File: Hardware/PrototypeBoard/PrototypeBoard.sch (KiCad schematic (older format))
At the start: 10 parts

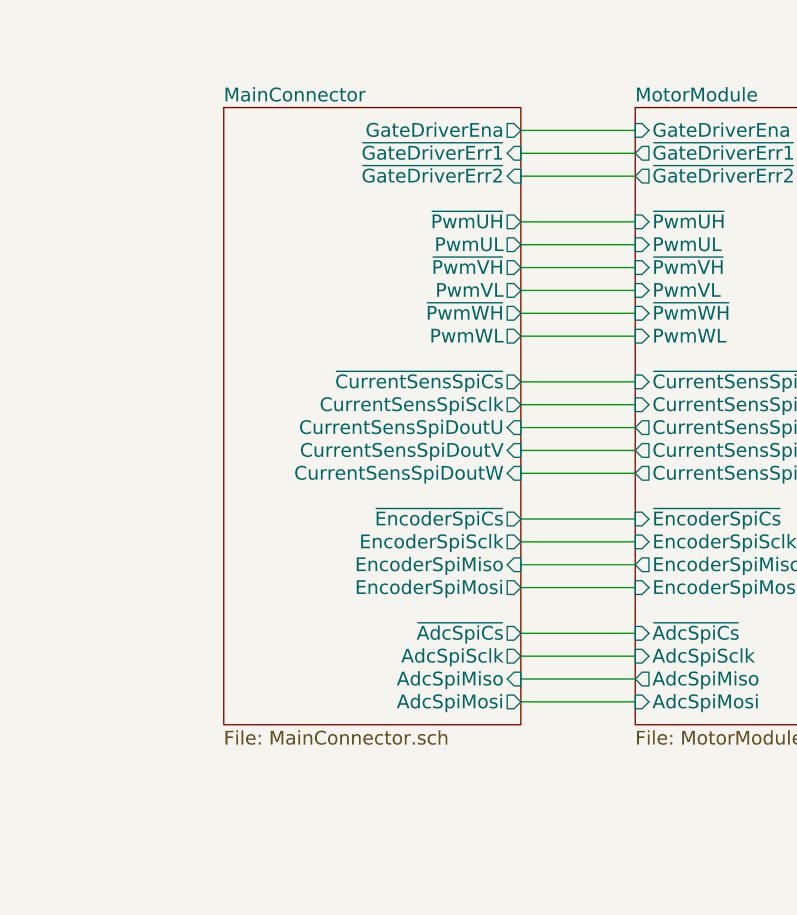
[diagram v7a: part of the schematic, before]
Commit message: Added LEDs for PWM, SPI communication, Gate Driver Errors and Gate Driver disabled
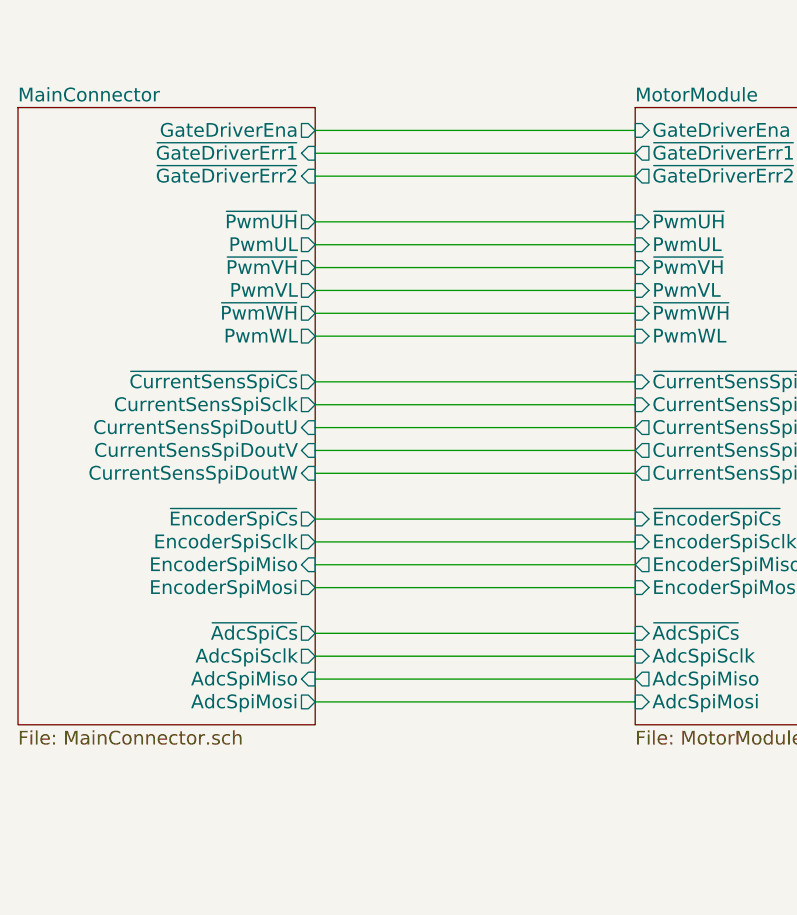
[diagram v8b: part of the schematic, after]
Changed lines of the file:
@@
 $EndSheet
 $Sheet
-S 4500 1800 1300 2700
+S 3600 1800 1300 2700
 U 5AFD76B5
 F0 "MainConnector" 60
 F1 "MainConnector.sch" 60
-F2 "GateDriverEna" O R 5800 1900 60
-F3 "~GateDriverErr1" I R 5800 2000 60
-F4 "~GateDriverErr2" I R 5800 2100 60
-F5 "~PwmUH" O R 5800 2300 60
-F6 "PwmUL" O R 5800 2400 60
-F7 "~PwmVH" O R 5800 2500 60
-F8 "PwmVL" O R 5800 2600 60
-F9 "~PwmWH" O R 5800 2700 60
-F10 "PwmWL" O R 5800 2800 60
-F11 "~CurrentSensSpiCs" O R 5800 3000 60
-F12 "CurrentSensSpiSclk" O R 5800 3100 60
-F13 "CurrentSensSpiDoutU" I R 5800 3200 60
-F14 "CurrentSensSpiDoutV" I R 5800 3300 60
-F15 "CurrentSensSpiDoutW" I R 5800 3400 60
-F16 "~EncoderSpiCs" O R 5800 3600 60
-F17 "EncoderSpiSclk" O R 5800 3700 60
-F18 "EncoderSpiMiso" I R 5800 3800 60
-F19 "EncoderSpiMosi" O R 5800 3900 60
-F20 "~AdcSpiCs" O R 5800 4100 60
-F21 "AdcSpiSclk" O R 5800 4200 60
-F22 "AdcSpiMiso" I R 5800 4300 60
-F23 "AdcSpiMosi" O R 5800 4400 60
+F2 "GateDriverEna" O R 4900 1900 60
+F3 "~GateDriverErr1" I R 4900 2000 60
+F4 "~GateDriverErr2" I R 4900 2100 60
+F5 "~PwmUH" O R 4900 2300 60
+F6 "PwmUL" O R 4900 2400 60
+F7 "~PwmVH" O R 4900 2500 60
+F8 "PwmVL" O R 4900 2600 60
+F9 "~PwmWH" O R 4900 2700 60
+F10 "PwmWL" O R 4900 2800 60
+F11 "~CurrentSensSpiCs" O R 4900 3000 60
+F12 "CurrentSensSpiSclk" O R 4900 3100 60
+F13 "CurrentSensSpiDoutU" I R 4900 3200 60
+F14 "CurrentSensSpiDoutV" I R 4900 3300 60
+F15 "CurrentSensSpiDoutW" I R 4900 3400 60
+F16 "~EncoderSpiCs" O R 4900 3600 60
+F17 "EncoderSpiSclk" O R 4900 3700 60
+F18 "EncoderSpiMiso" I R 4900 3800 60
+F19 "EncoderSpiMosi" O R 4900 3900 60
+F20 "~AdcSpiCs" O R 4900 4100 60
+F21 "AdcSpiSclk" O R 4900 4200 60
+F22 "AdcSpiMiso" I R 4900 4300 60
+F23 "AdcSpiMosi" O R 4900 4400 60
 $EndSheet
-Wire Wire Line
-	5800 1900 6300 1900
-Wire Wire Line
-	5800 2000 6300 2000
-Wire Wire Line
-	5800 2100 6300 2100
-Wire Wire Line
-	5800 2300 6300 2300
-Wire Wire Line
-	5800 2400 6300 2400
-Wire Wire Line
-	5800 2500 6300 2500
-Wire Wire Line
-	5800 2600 6300 2600
-Wire Wire Line
-	5800 2700 6300 2700
-Wire Wire Line
-	5800 2800 6300 2800
-Wire Wire Line
-	5800 3000 6300 3000
-Wire Wire Line
-	5800 3100 6300 3100
-Wire Wire Line
-	5800 3200 6300 3200
-Wire Wire Line
-	5800 3300 6300 3300
-Wire Wire Line
-	5800 3400 6300 3400
-Wire Wire Line
-	5800 3600 6300 3600
-Wire Wire Line
-	5800 3700 6300 3700
-Wire Wire Line
-	5800 3800 6300 3800
-Wire Wire Line
-	5800 3900 6300 3900
-Wire Wire Line
-	5800 4100 6300 4100
-Wire Wire Line
-	5800 4200 6300 4200
-Wire Wire Line
-	5800 4300 6300 4300
-Wire Wire Line
-	5800 4400 6300 4400
 $Comp
 L power:+3.3V #PWR03
@@
 $EndComp
 $Comp
-L power:GND #PWR?
+L power:GND #PWR01
 U 1 1 5B8A531B
 P 9000 4600
-F 0 "#PWR?" H 9000 4350 50  0001 C CNN
+F 0 "#PWR01" H 9000 4350 50  0001 C CNN
 F 1 "GND" H 9000 4450 50  0000 C CNN
 F 2 "" H 9000 4600 50  0001 C CNN
@@
 $EndComp
 $Comp
-L power:GND #PWR?
+L power:GND #PWR05
 U 1 1 5B8A53AC
 P 10100 4600
-F 0 "#PWR?" H 10100 4350 50  0001 C CNN
+F 0 "#PWR05" H 10100 4350 50  0001 C CNN
 F 1 "GND" H 10100 4450 50  0000 C CNN
 F 2 "" H 10100 4600 50  0001 C CNN
@@
 $EndComp
 $Comp
-L power:GND #PWR?
+L power:GND #PWR06
 U 1 1 5B8A53CB
 P 10100 5200
-F 0 "#PWR?" H 10100 4950 50  0001 C CNN
+F 0 "#PWR06" H 10100 4950 50  0001 C CNN
 F 1 "GND" H 10100 5050 50  0000 C CNN
 F 2 "" H 10100 5200 50  0001 C CNN
@@
 $EndComp
 $Comp
-L power:GND #PWR?
+L power:GND #PWR02
 U 1 1 5B8A53EA
 P 9000 5200
-F 0 "#PWR?" H 9000 4950 50  0001 C CNN
+F 0 "#PWR02" H 9000 4950 50  0001 C CNN
 F 1 "GND" H 9000 5050 50  0000 C CNN
 F 2 "" H 9000 5200 50  0001 C CNN
@@
 	1    0    0    -1
 $EndComp
+Wire Wire Line
+	4900 1900 6300 1900
+Wire Wire Line
+	4900 2000 6300 2000
+Wire Wire Line
+	4900 2100 6300 2100
+Wire Wire Line
+	4900 2300 6300 2300
+Wire Wire Line
+	4900 2400 6300 2400
+Wire Wire Line
+	4900 2500 6300 2500
+Wire Wire Line
+	4900 2600 6300 2600
+Wire Wire Line
+	4900 2700 6300 2700
+Wire Wire Line
+	4900 2800 6300 2800
+Wire Wire Line
+	4900 3000 6300 3000
+Wire Wire Line
+	4900 3100 6300 3100
+Wire Wire Line
+	4900 3200 6300 3200
+Wire Wire Line
+	4900 3300 6300 3300
+Wire Wire Line
+	4900 3400 6300 3400
+Wire Wire Line
+	4900 3600 6300 3600
+Wire Wire Line
+	4900 3700 6300 3700
+Wire Wire Line
+	4900 3800 6300 3800
+Wire Wire Line
+	4900 3900 6300 3900
+Wire Wire Line
+	4900 4100 6300 4100
+Wire Wire Line
+	4900 4200 6300 4200
+Wire Wire Line
+	4900 4300 6300 4300
+Wire Wire Line
+	4900 4400 6300 4400
 $EndSCHEMATC
